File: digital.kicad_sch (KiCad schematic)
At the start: 0 parts

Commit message: Dodanie części cyfrowej i procesora stm32g4
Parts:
- added Cain1, Cin1, Cin2, Cin3, Cm: 100n, symbol Device:C
- added Cain2: >1uF, symbol Device:C_Polarized
- added Cc: 10n, symbol Device:C
- added Cref: 10uF, symbol Device:C
- added D1: ESD5Zxx, Diode_SMD:D_SOD-523, symbol Diode:ESD5Zxx
- added Dm, Dm1: BAT54S, Package_TO_SOT_SMD:SOT-23, symbol Diode:BAT54S
- added J1: Conn_01x05_Pin, symbol Connector:Conn_01x05_Pin
- added Rain: 10, symbol Device:R
- added Rc: 1k, symbol Device:R
- added Rm1: 27k, symbol Device:R
- added Rm2: 3k, symbol Device:R
- added Rpwm: 22, symbol Device:R
- added Rpwmd: 10k, symbol Device:R
- added SW1: Voltage, symbol Device:RotaryEncoder_Switch_MP
- added SW2: Current, symbol Device:RotaryEncoder_Switch_MP
- added U1: STM32G431CBTx, Package_QFP:LQFP-48_7x7mm_P0.5mm, symbol MCU_ST_STM32G4:STM32G431CBTx
- added U2: REF3030, Package_TO_SOT_SMD:SOT-23, symbol Reference_Voltage:REF3030
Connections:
- new net: Cain1.1, Cain2.1, Rain.2, U1.21 (VDDA), U2.1 (IN)
- new net: Rpwm.1, Rpwmd.2, U1.30 (PA8)
- new net: SW2.A, U1.41 (PB4)
- new net: SW2.B, U1.42 (PB5)
- new net: Cref.2, U1.20 (VREF+), U2.2 (OUT)
- new net: SW1.A, U1.8 (PA0)
- new net: SW1.B, U1.9 (PA1)
- new net: Cref.1, U2.3 (GND)
- new net 3.3V: Cin1.2, Cin2.2, Cin3.2, D1.1 (K), Dm.2 (K), Dm1.2 (K), J1.5 (Pin_5), Rain.1, U1.1 (VBAT), U1.24 (VDD), U1.36 (VDD), U1.48 (VDD)
- new net CurrentMeasure: Cc.1, Dm1.3 (COM), Rc.2, U1.27 (PB13)
- new net GND: Cain1.2, Cain2.2, Cc.2, Cm.2, D1.2 (A), Dm.1 (A), Dm1.1 (A), Rm2.2, SW1.MP, SW2.MP, U1.19 (VSSA)
- new net GNDD: Cin1.1, Cin2.1, Cin3.1, J1.1 (Pin_1), Rpwmd.1, SW1.C, SW1.S1, SW2.C, SW2.S1, U1.23 (VSS), U1.35 (VSS), U1.47 (VSS)
- new net LCD_SPI1_CS: U1.12 (PA4)
- new net LCD_SPI1_MISO: U1.14 (PA6)
- new net LCD_SPI1_MOSI: U1.15 (PA7)
- new net LCD_SPI1_SCK: U1.13 (PA5)
- new net OUT_GND: Rc.1
- new net OutVoltageMeasure: Cm.1, Dm.3 (COM), Rm1.2, Rm2.1, U1.26 (PB12)
- new net PC_UART_RX: U1.11 (PA3)
- new net PC_UART_TX: U1.10 (PA2)
- new net PWM_IN: Rpwm.2
- new net RST: J1.4 (Pin_4), U1.7 (PG10)
- new net SWCLK: J1.2 (Pin_2), U1.38 (PA14)
- new net SWDIO: J1.3 (Pin_3), U1.37 (PA13)
- new net Vinm: Rm1.1
- no-connect marks 0 -> 22

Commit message: dodanie testpointów, diody tvs, rezystora pomiarowego
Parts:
- added TP_GND, TP_GNDD, TP_pwm_przed_r, TP_pwm_za_r: Conn_01x01_Pin, symbol Connector:Conn_01x01_Pin
- added jumper: 0, symbol Device:R
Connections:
- net GND: now also Cref.1, U2.3 (GND), TP_GND.1 (Pin_1), jumper.2
- net GNDD: now also TP_GNDD.1 (Pin_1), jumper.1
- net PWM_IN: now also TP_pwm_za_r.1 (Pin_1)
- net at Rpwm.1, Rpwmd.2, U1.30 (PA8): now also TP_pwm_przed_r.1 (Pin_1)
- net OUT_GND renamed OUT_GND_i_mesure

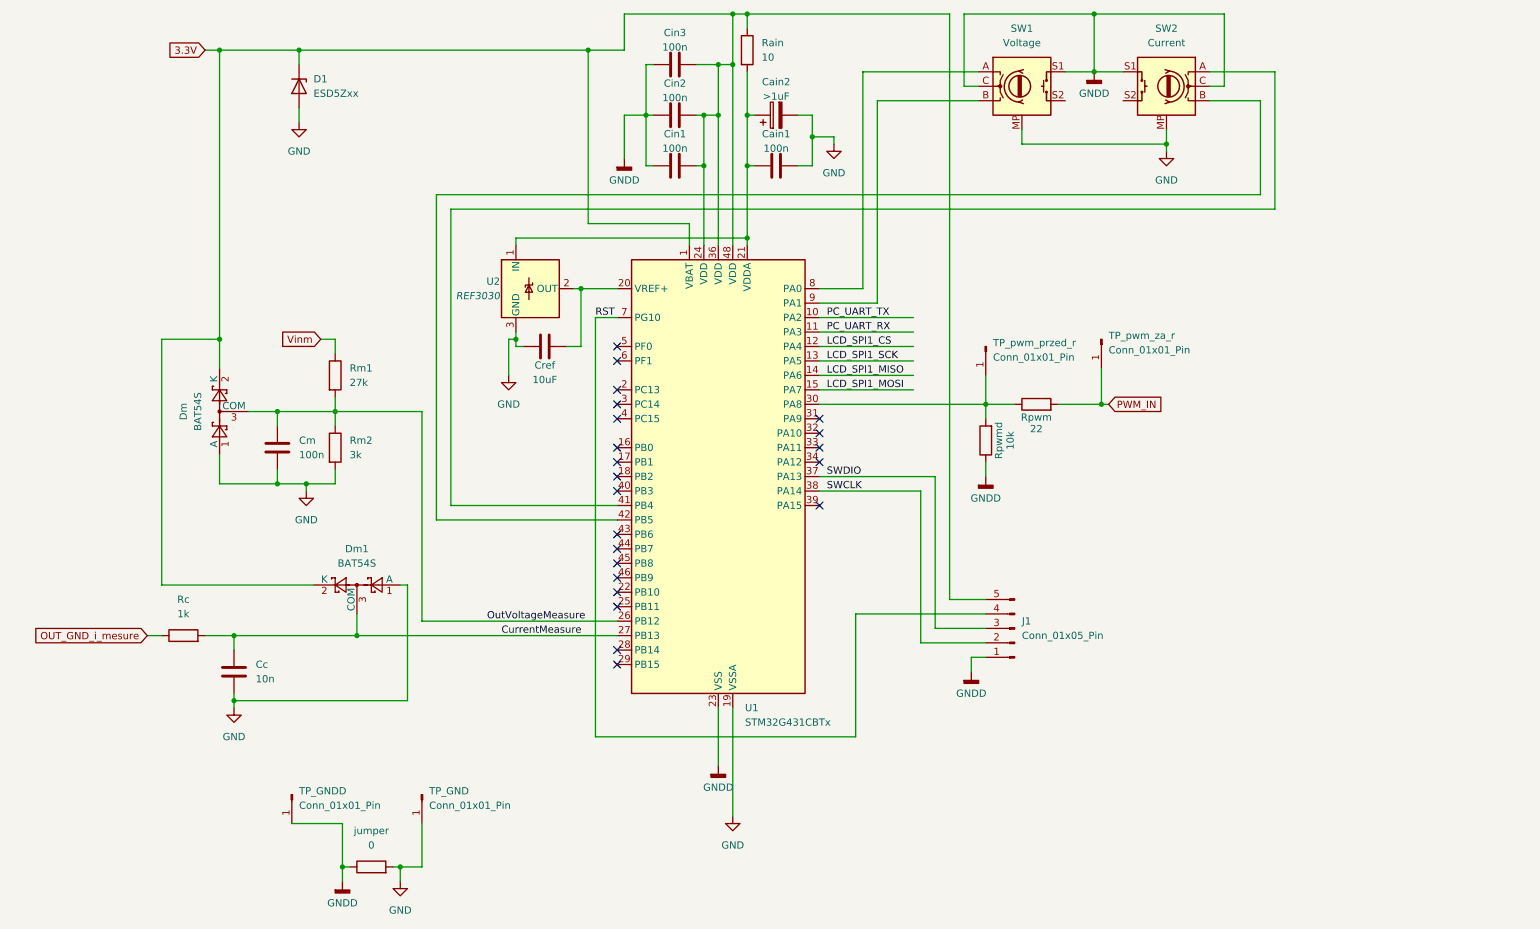
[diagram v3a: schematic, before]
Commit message: Dodanie złącza pinowego do wyświetlacza Ili9488 i złącza uart oraz numeracja elementów
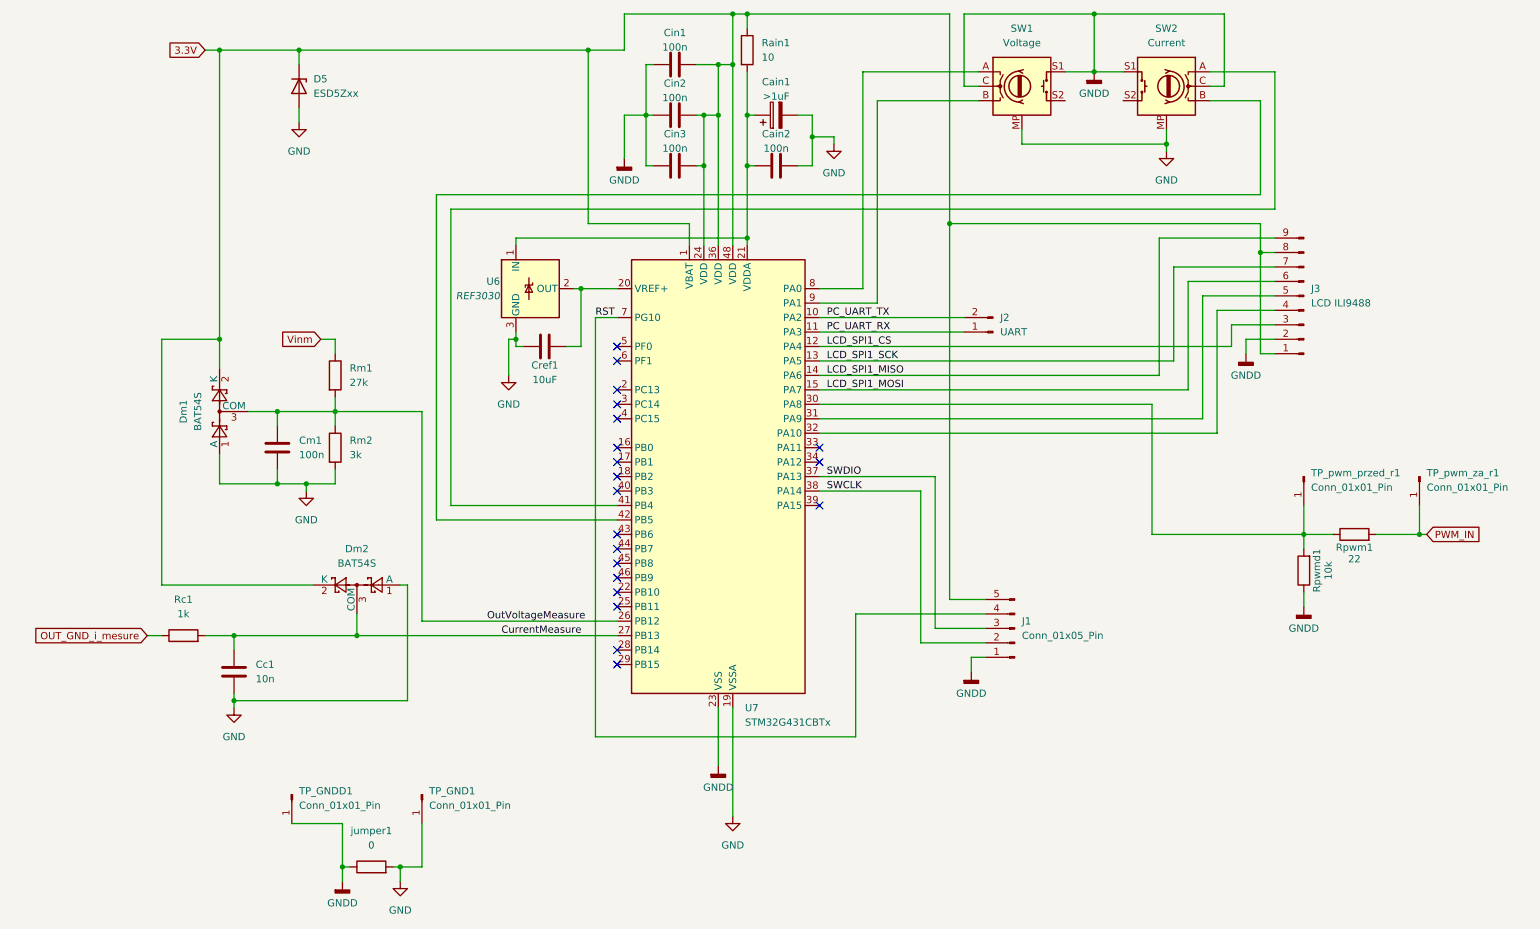
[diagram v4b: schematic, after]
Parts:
- added J2: UART, symbol Connector:Conn_01x02_Pin
- added J3: LCD ILI9488, symbol Connector:Conn_01x09_Pin
- renumbered Cain2 to Cain1, Cain1 to Cain2, Cc to Cc1, Cin3 to Cin1, Cin1 to Cin3, Cm to Cm1, Cref to Cref1, D1 to D5, Dm to Dm1, Dm1 to Dm2, Rain to Rain1, Rc to Rc1, Rpwm to Rpwm1, Rpwmd to Rpwmd1, TP_GND to TP_GND1, TP_GNDD to TP_GNDD1, TP_pwm_przed_r to TP_pwm_przed_r1, TP_pwm_za_r to TP_pwm_za_r1, U2 to U6, U1 to U7, jumper to jumper1
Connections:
- net 3.3V: now also J3.1 (Pin_1), J3.8 (Pin_8)
- net GNDD: now also J3.2 (Pin_2)
- net LCD_SPI1_CS: now also J3.3 (Pin_3)
- net LCD_SPI1_MISO: now also J3.9 (Pin_9)
- net LCD_SPI1_MOSI: now also J3.6 (Pin_6)
- net LCD_SPI1_SCK: now also J3.7 (Pin_7)
- net PC_UART_RX: now also J2.1 (Pin_1)
- net PC_UART_TX: now also J2.2 (Pin_2)
- net at U7.31 (PA9): now also J3.5 (Pin_5)
- net at U7.32 (PA10): now also J3.4 (Pin_4)
- no-connect marks 22 -> 20
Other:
- moved on the sheet: Rpwm1, Rpwmd1, TP_pwm_przed_r1, TP_pwm_za_r1

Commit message: dodanie footprintów do main buck (jeszcze driver i razystor bramek) poprawiony pinout LDI75L12UA, dodane footprinty do digital power
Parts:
- Cain2, Cc1, Cin1, Cin2, Cin3, Cm1, Cref1: footprint (none) -> Capacitor_SMD:C_0805_2012Metric_Pad1.18x1.45mm_HandSolder
- TP_GND1, TP_GNDD1, TP_pwm_przed_r1, TP_pwm_za_r1: footprint (none) -> Connector_PinHeader_2.54mm:PinHeader_1x01_P2.54mm_Vertical
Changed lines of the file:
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@@
 			)
 		)
-		(property "Footprint" ""
+		(property "Footprint" "Capacitor_SMD:C_0805_2012Metric_Pad1.18x1.45mm_HandSolder"
 			(at 59.3852 138.43 0)
 			(hide yes)
@@
 			)
 		)
-		(property "Footprint" ""
+		(property "Footprint" "Capacitor_SMD:C_0805_2012Metric_Pad1.18x1.45mm_HandSolder"
 			(at 67.0052 99.06 0)
 			(hide yes)
@@
 			)
 		)
-		(property "Footprint" ""
+		(property "Footprint" "Capacitor_SMD:C_0805_2012Metric_Pad1.18x1.45mm_HandSolder"
 			(at 157.48 44.7548 0)
 			(hide yes)
@@
 			)
 		)
-		(property "Footprint" ""
+		(property "Footprint" "Connector_PinHeader_2.54mm:PinHeader_1x01_P2.54mm_Vertical"
 			(at 246.38 100.33 0)
 			(hide yes)
@@
 			)
 		)
-		(property "Footprint" ""
+		(property "Footprint" "Capacitor_SMD:C_0805_2012Metric_Pad1.18x1.45mm_HandSolder"
 			(at 139.7 26.9748 0)
 			(hide yes)
@@
 			)
 		)
-		(property "Footprint" ""
+		(property "Footprint" "Capacitor_SMD:C_0805_2012Metric_Pad1.18x1.45mm_HandSolder"
 			(at 116.84 76.5048 0)
 			(hide yes)
@@
 			)
 		)
-		(property "Footprint" ""
+		(property "Footprint" "Capacitor_SMD:C_0805_2012Metric_Pad1.18x1.45mm_HandSolder"
 			(at 139.7 44.7548 0)
 			(hide yes)
@@
 			)
 		)
-		(property "Footprint" ""
+		(property "Footprint" "Connector_PinHeader_2.54mm:PinHeader_1x01_P2.54mm_Vertical"
 			(at 91.44 156.21 0)
 			(hide yes)
@@
 			)
 		)
-		(property "Footprint" ""
+		(property "Footprint" "Capacitor_SMD:C_0805_2012Metric_Pad1.18x1.45mm_HandSolder"
 			(at 139.7 35.8648 0)
 			(hide yes)
@@
 			)
 		)
-		(property "Footprint" ""
+		(property "Footprint" "Connector_PinHeader_2.54mm:PinHeader_1x01_P2.54mm_Vertical"
 			(at 68.58 156.21 0)
 			(hide yes)
@@
 			)
 		)
-		(property "Footprint" ""
+		(property "Footprint" "Connector_PinHeader_2.54mm:PinHeader_1x01_P2.54mm_Vertical"
 			(at 266.7 100.33 0)
 			(hide yes)

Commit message: Dodanie brakującego połączenia do przycisków enkoderów
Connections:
- net at SW2.S2: now also U7.34 (PA12)
- net at U7.33 (PA11): now also SW1.S2
- no-connect marks 20 -> 18
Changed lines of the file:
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@@
-	)
-	(no_connect
-		(at 161.29 97.79)
 	)
 	(no_connect
@@
 		(at 125.73 87.63)
 	)
-	(no_connect
-		(at 161.29 95.25)
-	)
 	(wire
 		(pts
@@
 	(wire
 		(pts
+			(xy 208.28 34.29) (xy 214.63 34.29)
+		)
+		(stroke
+			(width 0)
+			(type default)
+		)
+	)
+	(wire
+		(pts
 			(xy 148.59 21.59) (xy 148.59 19.05)
 		)
@@
 	(wire
 		(pts
+			(xy 208.28 97.79) (xy 208.28 34.29)
+		)
+		(stroke
+			(width 0)
+			(type default)
+		)
+	)
+	(wire
+		(pts
 			(xy 232.41 19.05) (xy 209.55 19.05)
 		)
@@
 	(wire
 		(pts
+			(xy 161.29 97.79) (xy 208.28 97.79)
+		)
+		(stroke
+			(width 0)
+			(type default)
+		)
+	)
+	(wire
+		(pts
 			(xy 140.97 36.83) (xy 139.7 36.83)
 		)
@@
 	(wire
 		(pts
+			(xy 205.74 95.25) (xy 205.74 34.29)
+		)
+		(stroke
+			(width 0)
+			(type default)
+		)
+	)
+	(wire
+		(pts
 			(xy 43.18 128.27) (xy 45.72 128.27)
 		)
@@
 	(wire
 		(pts
+			(xy 161.29 95.25) (xy 205.74 95.25)
+		)
+		(stroke
+			(width 0)
+			(type default)
+		)
+	)
+	(wire
+		(pts
 			(xy 140.97 36.83) (xy 140.97 45.72)
 		)
@@
 		)
 		(stroke
+			(width 0)
+			(type default)
+		)
+	)
+	(wire
+		(pts
+			(xy 205.74 34.29) (xy 204.47 34.29)
+		)
+		(stroke

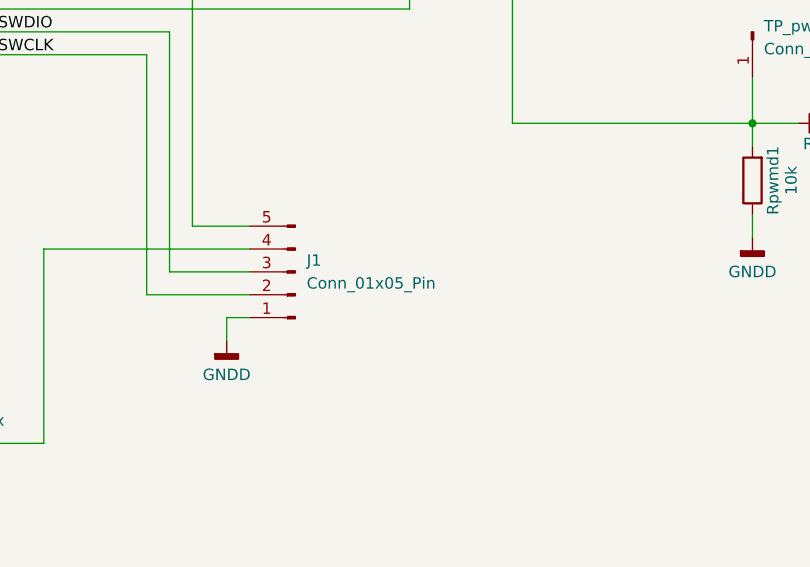
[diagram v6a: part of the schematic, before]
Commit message: Przydzielenie brakujących footprintów dla części cyfrowej oprócz enkoderów
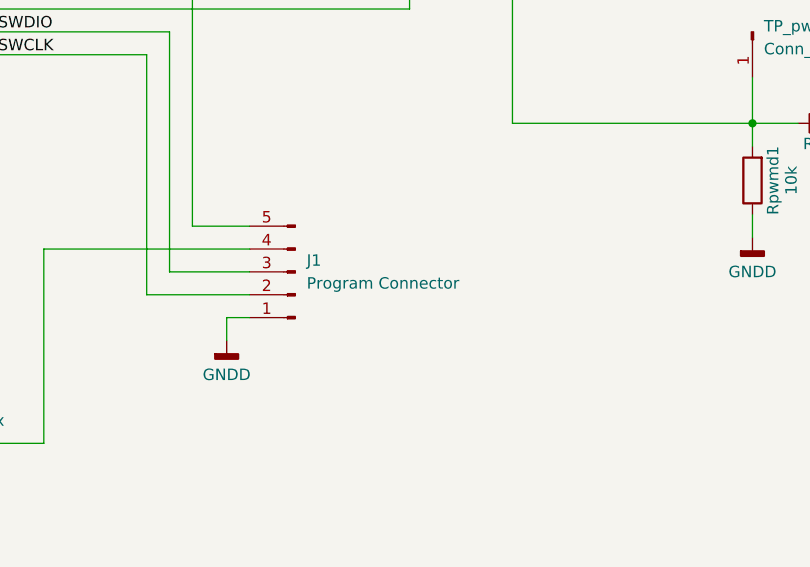
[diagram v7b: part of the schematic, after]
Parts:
- Cain1: footprint (none) -> Capacitor_SMD:C_0805_2012Metric_Pad1.18x1.45mm_HandSolder
- J1: value Conn_01x05_Pin -> Program Connector; footprint (none) -> Connector_PinHeader_2.54mm:PinHeader_1x05_P2.54mm_Vertical
- J2: footprint (none) -> Connector_PinHeader_2.54mm:PinHeader_1x02_P2.54mm_Vertical
- J3: footprint (none) -> Connector_PinHeader_2.54mm:PinHeader_1x09_P2.54mm_Vertical
- Rain1, Rc1, Rm1, Rm2, Rpwm1, Rpwmd1, jumper1: footprint (none) -> Resistor_SMD:R_0805_2012Metric_Pad1.20x1.40mm_HandSolder
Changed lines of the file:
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@@
 			)
 		)
-		(property "Footprint" ""
+		(property "Footprint" "Resistor_SMD:R_0805_2012Metric_Pad1.20x1.40mm_HandSolder"
 			(at 146.812 25.4 90)
 			(hide yes)
@@
 			)
 		)
-		(property "Footprint" ""
+		(property "Footprint" "Resistor_SMD:R_0805_2012Metric_Pad1.20x1.40mm_HandSolder"
 			(at 82.55 170.688 90)
 			(hide yes)
@@
 			)
 		)
-		(property "Footprint" ""
+		(property "Footprint" "Resistor_SMD:R_0805_2012Metric_Pad1.20x1.40mm_HandSolder"
 			(at 74.422 95.25 90)
 			(hide yes)
@@
 			)
 		)
-		(property "Footprint" ""
+		(property "Footprint" "Resistor_SMD:R_0805_2012Metric_Pad1.20x1.40mm_HandSolder"
 			(at 74.422 82.55 90)
 			(hide yes)
@@
 			)
 		)
-		(property "Footprint" ""
+		(property "Footprint" "Resistor_SMD:R_0805_2012Metric_Pad1.20x1.40mm_HandSolder"
 			(at 255.27 112.268 90)
 			(hide yes)
@@
 			)
 		)
-		(property "Footprint" ""
+		(property "Footprint" "Resistor_SMD:R_0805_2012Metric_Pad1.20x1.40mm_HandSolder"
 			(at 49.53 130.048 90)
 			(hide yes)
@@
 			)
 		)
-		(property "Footprint" ""
+		(property "Footprint" "Connector_PinHeader_2.54mm:PinHeader_1x09_P2.54mm_Vertical"
 			(at 246.38 68.58 0)
 			(hide yes)
@@
 			)
 		)
-		(property "Footprint" ""
+		(property "Footprint" "Resistor_SMD:R_0805_2012Metric_Pad1.20x1.40mm_HandSolder"
 			(at 248.158 116.84 90)
 			(hide yes)
@@
 			)
 		)
-		(property "Value" "Conn_01x05_Pin"
+		(property "Value" "Program Connector"
 			(at 196.85 128.2699 0)
 			(show_name no)
@@
 			)
 		)
-		(property "Footprint" ""
+		(property "Footprint" "Connector_PinHeader_2.54mm:PinHeader_1x05_P2.54mm_Vertical"
 			(at 195.58 127 0)
 			(hide yes)
@@
 			)
 		)
-		(property "Footprint" ""
+		(property "Footprint" "Connector_PinHeader_2.54mm:PinHeader_1x02_P2.54mm_Vertical"
 			(at 191.77 74.93 0)
 			(hide yes)
@@
 			)
 		)
-		(property "Footprint" ""
+		(property "Footprint" "Capacitor_SMD:C_0805_2012Metric_Pad1.18x1.45mm_HandSolder"
 			(at 157.48 35.8648 0)
 			(hide yes)
